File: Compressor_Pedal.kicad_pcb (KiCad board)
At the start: 2 copper layers, 0 parts

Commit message: schematic finished, begin layout
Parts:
- added C1: 1uF, Capacitor_THT:C_Radial_D5.0mm_H11.0mm_P2.00mm, F.Cu at (92.0, 78.7)
- added C2: 100pF, Capacitor_THT:C_Disc_D5.0mm_W2.5mm_P2.50mm, F.Cu at (76.2, 114.3)
- added C3: 1nF, Capacitor_THT:C_Disc_D5.0mm_W2.5mm_P2.50mm, F.Cu at (150.0, 114.0)
- added D1: 1N4148, Diode_THT:D_DO-35_SOD27_P2.54mm_Vertical_KathodeUp, F.Cu at (76.2, 109.2)
- added D10: RED 1.7V, LED_THT:LED_D3.0mm_FlatTop, F.Cu at (132.0, 98.9)
- added D11: 1N4148, Diode_THT:D_DO-35_SOD27_P2.54mm_Vertical_KathodeUp, F.Cu at (119.7, 101.2)
- added D12: 1N4148, Diode_THT:D_DO-35_SOD27_P2.54mm_Vertical_KathodeUp, F.Cu at (119.7, 104.9)
- added D13: 1N4148, Diode_THT:D_DO-35_SOD27_P2.54mm_Vertical_KathodeUp, F.Cu at (119.7, 108.7)
- added D14: RED 1.7V, LED_THT:LED_D3.0mm_FlatTop, F.Cu at (132.0, 104.4)
- added D15: Blue 2.3V, LED_THT:LED_D3.0mm_Clear, F.Cu at (132.0, 110.0)
- added D2: 1N4148, Diode_THT:D_DO-35_SOD27_P2.54mm_Vertical_KathodeUp, F.Cu at (73.7, 111.8)
- added D3: 1N4148, Diode_THT:D_DO-35_SOD27_P2.54mm_Vertical_KathodeUp, F.Cu at (84.2, 72.6)
- added D4: 1N4148, Diode_THT:D_DO-35_SOD27_P2.54mm_Vertical_KathodeUp, F.Cu at (119.7, 78.5)
- added D5: 1N34A, Diode_THT:D_DO-35_SOD27_P2.54mm_Vertical_KathodeUp, F.Cu at (119.7, 82.3)
- added D6: 1N4148, Diode_THT:D_DO-35_SOD27_P2.54mm_Vertical_KathodeUp, F.Cu at (119.7, 86.1)
- added D7: 1N4148, Diode_THT:D_DO-35_SOD27_P2.54mm_Vertical_KathodeUp, F.Cu at (119.7, 89.8)
- added D8: 1N4148, Diode_THT:D_DO-35_SOD27_P2.54mm_Vertical_KathodeUp, F.Cu at (119.7, 93.6)
- added D9: 1N4148, Diode_THT:D_DO-35_SOD27_P2.54mm_Vertical_KathodeUp, F.Cu at (119.7, 97.4)
- added J1: InputJack, TestPoint:TestPoint_2Pads_Pitch5.08mm_Drill1.3mm, F.Cu at (78.7, 162.6)
- added J2: OutputJack, TestPoint:TestPoint_2Pads_Pitch5.08mm_Drill1.3mm, F.Cu at (91.4, 162.6)
- added J3: Sidechain, TestPoint:TestPoint_2Pads_Pitch5.08mm_Drill1.3mm, F.Cu at (71.1, 132.1)
- added Q1: PN2222A, Package_TO_SOT_THT:TO-92_Inline, F.Cu at (138.2, 111.2)
- added R1: 10k, Resistor_THT:R_Axial_DIN0207_L6.3mm_D2.5mm_P2.54mm_Vertical, F.Cu at (94.0, 114.3)
- added R10: 4.7k, Resistor_THT:R_Axial_DIN0207_L6.3mm_D2.5mm_P2.54mm_Vertical, F.Cu at (76.2, 134.6)
- added R11: 10k, Resistor_THT:R_Axial_DIN0207_L6.3mm_D2.5mm_P2.54mm_Vertical, F.Cu at (83.8, 157.5)
- added R12: 100k, Resistor_THT:R_Axial_DIN0207_L6.3mm_D2.5mm_P2.54mm_Vertical, F.Cu at (81.3, 139.7)
- added R13: 220k, Resistor_THT:R_Axial_DIN0207_L6.3mm_D2.5mm_P2.54mm_Vertical, F.Cu at (126.2, 78.7)
- added R14: 10k, Resistor_THT:R_Axial_DIN0207_L6.3mm_D2.5mm_P2.54mm_Vertical, F.Cu at (126.2, 82.7)
- added R15: 47k, Resistor_THT:R_Axial_DIN0207_L6.3mm_D2.5mm_P2.54mm_Vertical, F.Cu at (126.2, 86.8)
- added R16: 47k, Resistor_THT:R_Axial_DIN0207_L6.3mm_D2.5mm_P2.54mm_Vertical, F.Cu at (126.2, 90.8)
- added R17: 100k, Resistor_THT:R_Axial_DIN0207_L6.3mm_D2.5mm_P2.54mm_Vertical, F.Cu at (76.2, 152.4)
- added R18: 10k, Resistor_THT:R_Axial_DIN0207_L6.3mm_D2.5mm_P2.54mm_Vertical, F.Cu at (86.4, 160.0)
- added R19: 100k, Resistor_THT:R_Axial_DIN0207_L6.3mm_D2.5mm_P2.54mm_Vertical, F.Cu at (76.2, 129.5)
- added R2: 10k, Resistor_THT:R_Axial_DIN0207_L6.3mm_D2.5mm_P2.54mm_Vertical, F.Cu at (73.7, 116.8)
- added R20: 10k, Resistor_THT:R_Axial_DIN0207_L6.3mm_D2.5mm_P2.54mm_Vertical, F.Cu at (126.2, 94.9)
- added R21: 10k, Resistor_THT:R_Axial_DIN0207_L6.3mm_D2.5mm_P2.54mm_Vertical, F.Cu at (126.2, 98.9)
- added R3: 10k, Resistor_THT:R_Axial_DIN0207_L6.3mm_D2.5mm_P2.54mm_Vertical, F.Cu at (76.2, 119.4)
- added R4: 1k-4.7k, Resistor_THT:R_Axial_DIN0207_L6.3mm_D2.5mm_P2.54mm_Vertical, F.Cu at (73.0, 77.4)
- added R5: 100k, Resistor_THT:R_Axial_DIN0207_L6.3mm_D2.5mm_P2.54mm_Vertical, F.Cu at (73.7, 96.5)
- added R6: 100k, Resistor_THT:R_Axial_DIN0207_L6.3mm_D2.5mm_P2.54mm_Vertical, F.Cu at (94.0, 96.5)
- added R7: 100k, Resistor_THT:R_Axial_DIN0207_L6.3mm_D2.5mm_P2.54mm_Vertical, F.Cu at (96.5, 99.1)
- added R8: 100k, Resistor_THT:R_Axial_DIN0207_L6.3mm_D2.5mm_P2.54mm_Vertical, F.Cu at (96.5, 101.6)
- added R9: 33k, Resistor_THT:R_Axial_DIN0207_L6.3mm_D2.5mm_P2.54mm_Vertical, F.Cu at (94.0, 94.0)
- added RV1: B20k, Potentiometer_THT:Potentiometer_Alps_RK163_Single_Horizontal, F.Cu at (63.5, 67.9)
- added RV2: A20k, Potentiometer_THT:Potentiometer_Alps_RK163_Single_Horizontal, F.Cu at (63.5, 87.4)
- added RV3: B20k, Potentiometer_THT:Potentiometer_Alps_RK163_Single_Horizontal, F.Cu at (63.5, 106.8)
- added RV4: B20k, Potentiometer_THT:Potentiometer_Alps_RK163_Single_Horizontal, F.Cu at (149.9, 81.4)
- added RV5: A50k, Potentiometer_THT:Potentiometer_Alps_RK163_Single_Horizontal, F.Cu at (63.5, 129.7)
- added RV6: A150k, Potentiometer_THT:Potentiometer_Alps_RK163_Single_Horizontal, F.Cu at (63.5, 149.9)
- added SW1: SW_DPDT_x2, Button_Switch_THT:SW_NKK_GW12LJP, F.Cu at (149.9, 107.4)
- added TP1: abs_s1, Connector_Pin:Pin_D1.3mm_L10.0mm_W3.5mm_Flat, F.Cu at (81.3, 106.7)
- added TP2: abs_out, Connector_Pin:Pin_D1.3mm_L10.0mm_W3.5mm_Flat, F.Cu at (88.9, 106.7)
- added TP3: Envelope, Connector_Pin:Pin_D1.3mm_L10.0mm_W3.5mm_Flat, F.Cu at (81.3, 88.9)
- added TP4: Threshold, Connector_Pin:Pin_D1.3mm_L10.0mm_W3.5mm_Flat, F.Cu at (88.9, 88.9)
- added TP5: cv_in, Connector_Pin:Pin_D1.3mm_L10.0mm_W3.5mm_Flat, F.Cu at (150.7, 98.4)
- added TP6: cv_out, Connector_Pin:Pin_D1.3mm_L10.0mm_W3.5mm_Flat, F.Cu at (150.7, 103.1)
- added TP7: Mod, Connector_Pin:Pin_D1.3mm_L10.0mm_W3.5mm_Flat, F.Cu at (88.9, 139.7)
- added U1: LM358, Package_DIP:DIP-8_W7.62mm_Socket_LongPads, F.Cu at (81.3, 111.8)
- added U2: LM358, Package_DIP:DIP-8_W7.62mm_Socket_LongPads, F.Cu at (81.3, 94.0)
- added U3: LM358, Package_DIP:DIP-8_W7.62mm_Socket_LongPads, F.Cu at (138.3, 98.2)
- added U4: LM358, Package_DIP:DIP-8_W7.62mm_Socket_LongPads, F.Cu at (81.3, 144.8)
- added U5: LM358, Package_DIP:DIP-8_W7.62mm_Socket_LongPads, F.Cu at (81.3, 127.0)

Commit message: sent for build
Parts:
- added J4: Conn_01x03, Connector_PinHeader_2.54mm:PinHeader_1x03_P2.54mm_Vertical, F.Cu at (78.7, 157.5)
- added JP1: Jumper_2_Bridged, TestPoint:TestPoint_2Pads_Pitch2.54mm_Drill0.8mm, F.Cu at (76.2, 140.7)
- added JP2: Jumper_2_Bridged, TestPoint:TestPoint_2Pads_Pitch2.54mm_Drill0.8mm, F.Cu at (73.7, 143.3)
- added TP10: MOD_IN, Connector_Pin:Pin_D0.9mm_L10.0mm_W2.4mm_FlatFork, F.Cu at (104.1, 157.5)
- added TP8: AIN, Connector_Pin:Pin_D0.9mm_L10.0mm_W2.4mm_FlatFork, F.Cu at (99.1, 157.5)
- added TP9: AOUT, Connector_Pin:Pin_D0.9mm_L10.0mm_W2.4mm_FlatFork, F.Cu at (99.1, 162.6)
- RV1, RV2, RV3, RV4, RV5, RV6: footprint Potentiometer_THT:Potentiometer_Alps_RK163_Single_Horizontal -> CustomLibrary:Potentiometer_Alps_RK163_Single_Horizontal_Pads_Only
- SW1: footprint Button_Switch_THT:SW_NKK_GW12LJP -> CustomLibrary:SW_NKK_GW12LJP
- TP1: value abs_s1 -> ABS1; footprint Connector_Pin:Pin_D1.3mm_L10.0mm_W3.5mm_Flat -> Connector_Pin:Pin_D0.9mm_L10.0mm_W2.4mm_FlatFork
- TP2: value abs_out -> ABS2; footprint Connector_Pin:Pin_D1.3mm_L10.0mm_W3.5mm_Flat -> Connector_Pin:Pin_D0.9mm_L10.0mm_W2.4mm_FlatFork
- TP3: value Envelope -> ENV; footprint Connector_Pin:Pin_D1.3mm_L10.0mm_W3.5mm_Flat -> Connector_Pin:Pin_D0.9mm_L10.0mm_W2.4mm_FlatFork
- TP4: value Threshold -> THR; footprint Connector_Pin:Pin_D1.3mm_L10.0mm_W3.5mm_Flat -> Connector_Pin:Pin_D0.9mm_L10.0mm_W2.4mm_FlatFork
- TP5: value cv_in -> CV1; footprint Connector_Pin:Pin_D1.3mm_L10.0mm_W3.5mm_Flat -> Connector_Pin:Pin_D0.9mm_L10.0mm_W2.4mm_FlatFork
- TP6: value cv_out -> CV2; footprint Connector_Pin:Pin_D1.3mm_L10.0mm_W3.5mm_Flat -> Connector_Pin:Pin_D0.9mm_L10.0mm_W2.4mm_FlatFork
- TP7: value Mod -> MOD_OUT; footprint Connector_Pin:Pin_D1.3mm_L10.0mm_W3.5mm_Flat -> Connector_Pin:Pin_D0.9mm_L10.0mm_W2.4mm_FlatFork
- moved RV1 95.5 mm to (121.9, 143.4), turned to 180 degrees
- moved RV4 85.8 mm to (121.9, 162.5), turned to 180 degrees
- moved R14 76.8 mm to (94.0, 152.4)
- moved R15 76.7 mm to (114.3, 162.6)
- moved TP5 76.4 mm to (109.2, 162.6)
- moved D4 72.6 mm to (96.5, 147.3), turned to 180 degrees
- moved R16 70.2 mm to (114.3, 160.0)
- moved RV2 69.1 mm to (121.9, 124.4), turned to 180 degrees
- moved R13 69.0 mm to (94.0, 139.7)
- moved TP6 68.4 mm to (109.2, 157.5)
- moved D6 67.9 mm to (96.5, 149.9), turned to 180 degrees
- moved D5 66.7 mm to (96.5, 144.8), turned to 180 degrees
- moved C3 62.7 mm to (94.0, 142.2)
- moved R20 61.2 mm to (114.3, 154.9)
- moved D3 59.8 mm to (109.2, 127.0), turned to 180 degrees
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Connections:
- U5 pad 5: GNDA -> Net-(JP2-B)
- U5 pad 6: Net-(U5B--) -> Net-(JP1-A)
- U5 pad 7: Net-(U5B--) -> Net-(JP1-B)
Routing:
- net +9V: track 0.00 -> 118.5 mm
- net -9V: track 0.00 -> 97.7 mm, vias 0 -> 1
- net /Volume Control/vol_mod: track 0.00 -> 86.2 mm, vias 0 -> 2
- net Net-(U2A--): track 0.00 -> 71.6 mm, vias 0 -> 1
- net Net-(SW1A-B): track 0.00 -> 65.0 mm
- net Net-(R6-Pad2): track 0.00 -> 58.1 mm
- net /Volume Detector/signal_in: track 0.00 -> 57.5 mm, vias 0 -> 1
- net Net-(R9-Pad2): track 0.00 -> 57.2 mm
- net /output: track 0.00 -> 52.5 mm
- net /Volume Control/ctrl_voltage: track 0.00 -> 48.3 mm
- net Net-(U2A-+): track 0.00 -> 34.9 mm
- net Net-(U3A-+): track 0.00 -> 33.5 mm
- net Net-(SW1B-B): track 0.00 -> 31.7 mm, vias 0 -> 1
- net Net-(JP1-B): track 0.00 -> 28.9 mm
- net /input: track 0.00 -> 28.9 mm
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- added copper zone on B.Cu, net GNDA
- added copper zone on F.Cu, net GNDA
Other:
- board outline added: 60.5 x 52.8 mm
- board text added: "+"
- board text added: "+9V"
- board text added: "-9V"
- board text added: "Compressor Jacob Miller v0.1"
- board text added: "GND"
- board text added: "Germanium"

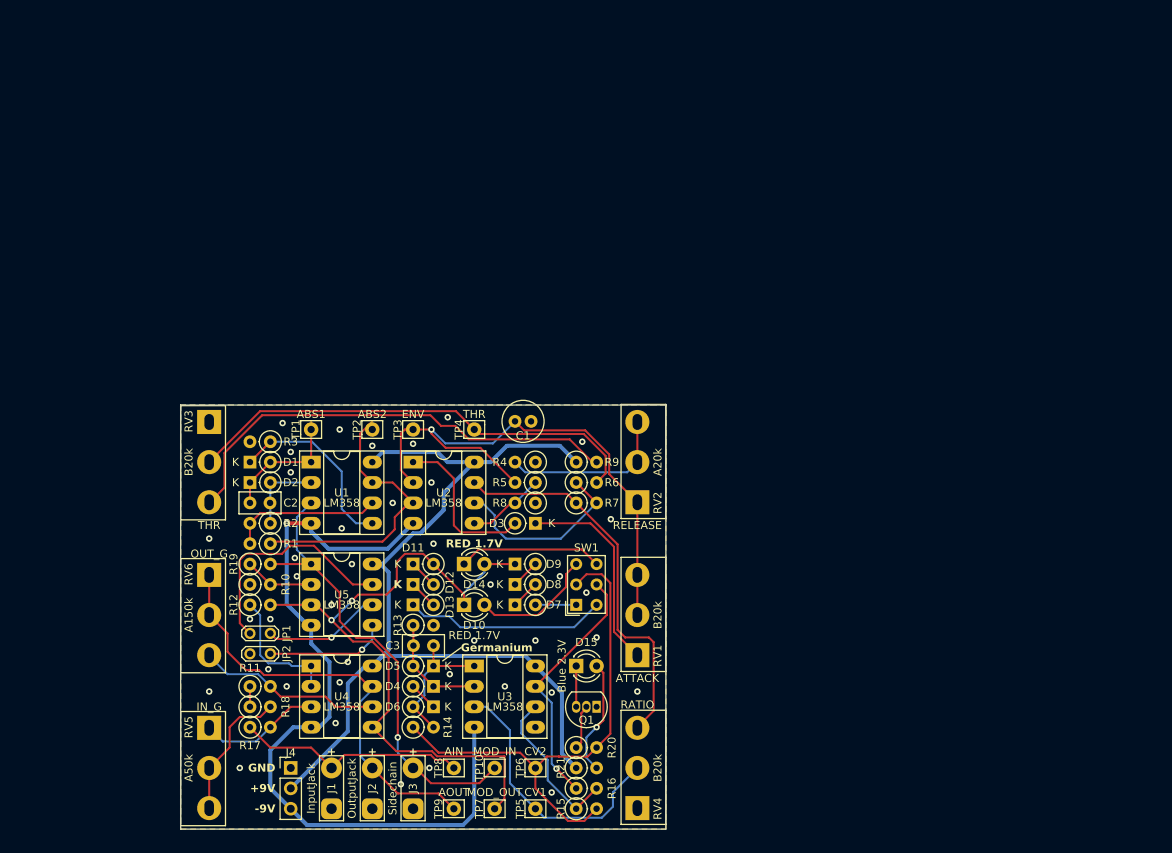
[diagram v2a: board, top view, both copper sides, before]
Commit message: updates first build to add missing external mod switch - moving to v0.2
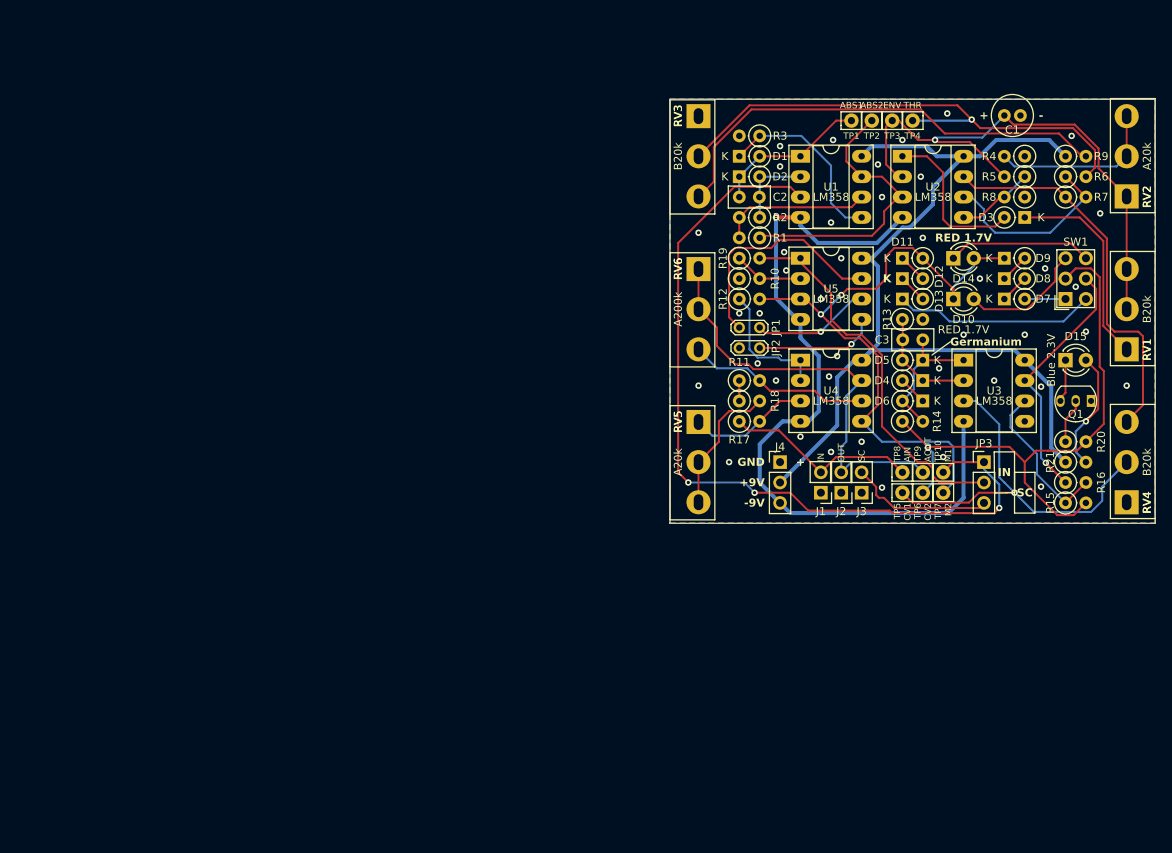
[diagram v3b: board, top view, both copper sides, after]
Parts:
- added JP3: Select, Connector_PinHeader_2.54mm:PinHeader_1x03_P2.54mm_Vertical, F.Cu at (165.1, 119.4)
- J1: value InputJack -> IN; footprint TestPoint:TestPoint_2Pads_Pitch5.08mm_Drill1.3mm -> Connector_PinHeader_2.54mm:PinHeader_1x02_P2.54mm_Vertical
- J2: value OutputJack -> OUT; footprint TestPoint:TestPoint_2Pads_Pitch5.08mm_Drill1.3mm -> Connector_PinHeader_2.54mm:PinHeader_1x02_P2.54mm_Vertical
- J3: value Sidechain -> SC; footprint TestPoint:TestPoint_2Pads_Pitch5.08mm_Drill1.3mm -> Connector_PinHeader_2.54mm:PinHeader_1x02_P2.54mm_Vertical
- R14: value 10k -> 1k
- R4: value 1k-4.7k -> 4.7k
- RV5: value A50k -> A20k
- RV6: value A150k -> A200k
- TP10: value MOD_IN -> M1
- TP7: value MOD_OUT -> M2
- moved TP1 77.5 mm to (148.6, 76.8)
- moved TP2 73.2 mm to (151.1, 76.8)
- moved J1 72.6 mm to (144.8, 123.2), turned to 180 degrees
- moved TP9 71.9 mm to (157.5, 120.7)
- moved D2 71.9 mm to (134.6, 83.8)
- moved Q1 71.9 mm to (177.8, 111.8)
- moved R10 71.9 mm to (134.6, 96.5)
- moved R17 71.9 mm to (134.6, 114.3)
- moved R18 71.9 mm to (134.6, 111.8)
- moved R19 71.9 mm to (134.6, 94.0)
- moved R5 71.9 mm to (170.2, 83.8)
- moved U5 71.9 mm to (142.2, 94.0)
- moved C2 71.9 mm to (137.1, 86.4)
- moved D1 71.9 mm to (134.6, 81.3)
- moved D3 71.9 mm to (170.2, 88.9)
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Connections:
- J3 pad 2: /Volume Detector/signal_in -> Net-(J3-T)
- R19 pad 2: /Volume Detector/signal_in -> Net-(JP3-C)
- U5 pad 1: /Volume Detector/signal_in -> Net-(JP3-C)
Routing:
- net Net-(JP3-C): track 0.00 -> 47.5 mm
- net /Volume Detector/signal_in: track 57.5 -> 101.7 mm, vias 1 -> 3
- net Net-(J3-T): track 0.00 -> 17.9 mm
- net Net-(U3A-+): track 33.5 -> 48.5 mm, vias 0 -> 1
- net Net-(R6-Pad2): track 58.1 -> 65.5 mm, vias 0 -> 1
- net Net-(SW1A-B): track 65.0 -> 71.9 mm, vias 0 -> 1
- net /Volume Control/vol_mod: track 86.2 -> 79.9 mm
- net /input: track 28.9 -> 24.5 mm
- net Net-(D1-A): track 16.3 -> 19.4 mm
- net Net-(U2A--): track 71.6 -> 70.2 mm
- net -9V: track 97.7 -> 96.3 mm
- net +9V: track 118.5 -> 117.6 mm
- net Net-(D15-A): track 14.5 -> 15.0 mm
- net GNDA: vias 40 -> 41
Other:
- board text added: "-"
- board text added: "Compressor Jacob Miller v0.2"
- board text added: "IN"
- board text added: "SC"
- board text removed: "Compressor Jacob Miller v0.1"

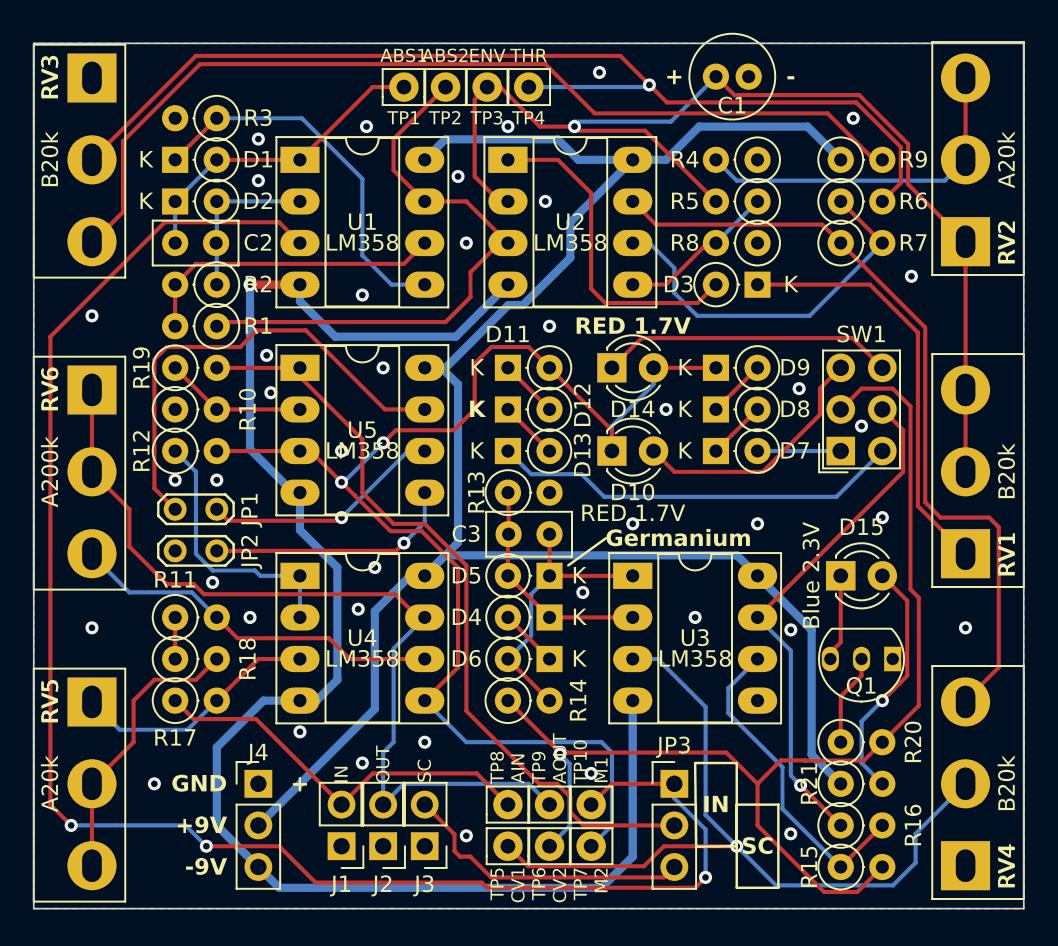
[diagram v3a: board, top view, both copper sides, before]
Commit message: fix problem with external input
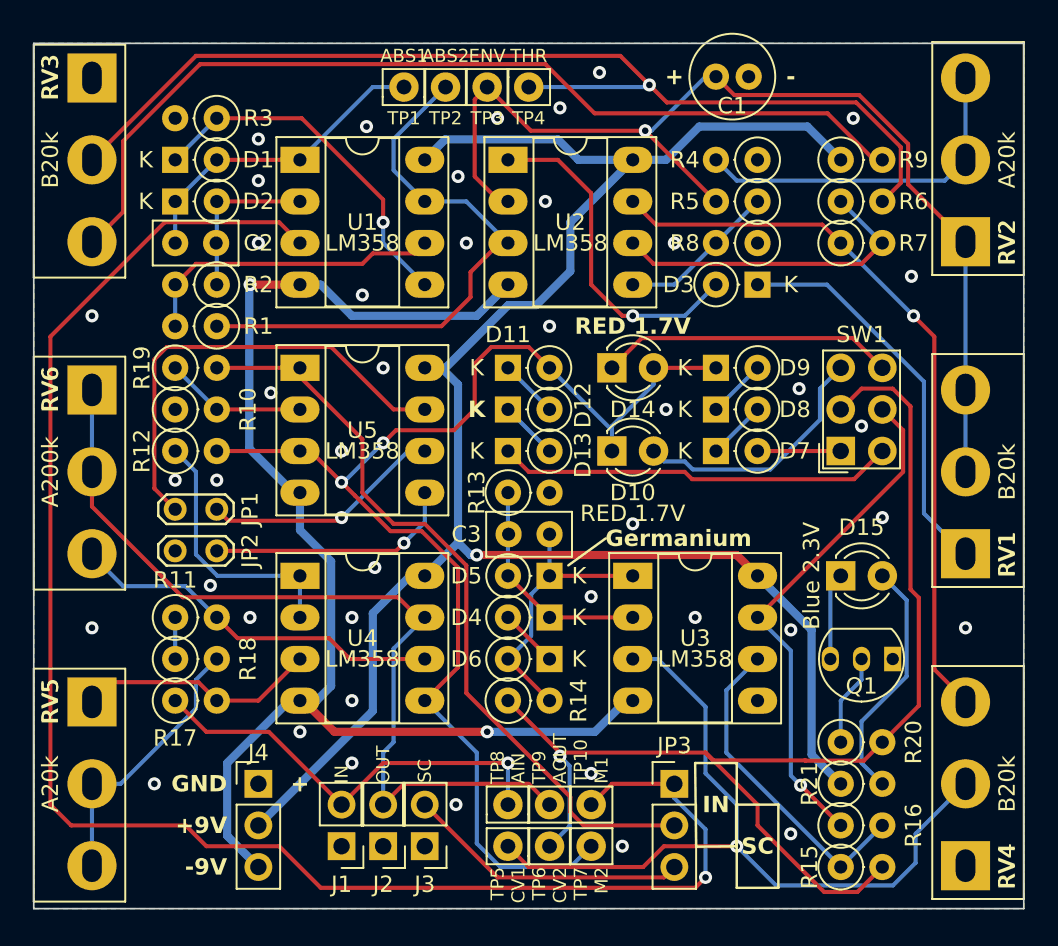
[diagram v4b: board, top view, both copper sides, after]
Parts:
- Q1: footprint Package_TO_SOT_THT:TO-92_Inline -> CustomLibrary:TO-92_Inline_wide
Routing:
- net -9V: track 96.3 -> 81.1 mm, vias 1 -> 2
- net Net-(U2A--): track 70.2 -> 65.4 mm
- net /Volume Control/ctrl_voltage: track 48.3 -> 44.8 mm, vias 0 -> 1
- net Net-(U2B--): track 22.4 -> 19.9 mm
- net /Volume Control/vol_mod: track 79.9 -> 77.8 mm
- net Net-(SW1A-B): track 71.9 -> 74.0 mm
- net /input: track 24.5 -> 26.5 mm, vias 0 -> 1
- net +9V: track 117.6 -> 115.8 mm, vias 0 -> 1
- net Net-(D3-K): track 25.7 -> 24.3 mm
- net /output: track 52.4 -> 53.6 mm
- net Net-(D1-K): track 23.2 -> 22.1 mm, vias 0 -> 1
- net Net-(U4A-+): track 13.7 -> 14.7 mm
- net Net-(D13-K): track 25.2 -> 24.3 mm
- net Net-(JP1-B): track 28.9 -> 28.1 mm
- net Net-(JP3-C): track 47.5 -> 46.9 mm
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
